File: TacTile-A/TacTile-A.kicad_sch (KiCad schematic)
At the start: 100 parts, among them J1 Conn_01x01, J2 Conn_01x01, J3 Conn_01x01, J4 Conn_01x01, U1 MCP14A0304xMNY, U10 MCP14A0304xMNY, U11 MCP14A0304xMNY, U12 MCP14A0304xMNY, U13 MCP14A0304xMNY, U14 MCP14A0304xMNY, U15 MCP14A0304xMNY, U16 MCP14A0304xMNY, U2 MCP14A0304xMNY, U3 MCP14A0304xMNY, U4 MCP14A0304xMNY, U5 MCP14A0304xMNY, U6 MCP14A0304xMNY, U7 MCP14A0304xMNY, U8 MCP14A0304xMNY, U9 MCP14A0304xMNY

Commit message: Swapped headers and sockets on board A
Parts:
- J1, J3: footprint Connector_PinHeader_2.00mm:PinHeader_1x01_P2.00mm_Horizontal -> Connector_PinSocket_2.00mm:PinSocket_1x01_P2.00mm_Horizontal
- J2, J4: footprint Connector_PinSocket_2.00mm:PinSocket_1x01_P2.00mm_Horizontal -> Connector_PinHeader_2.00mm:PinHeader_1x01_P2.00mm_Horizontal

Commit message: Enlarged grounding pins on board A
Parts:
- J1, J3: footprint Connector_PinSocket_2.00mm:PinSocket_1x01_P2.00mm_Horizontal -> Connector_PinSocket_2.54mm:PinSocket_1x01_P2.54mm_Horizontal
- J2, J4: footprint Connector_PinHeader_2.00mm:PinHeader_1x01_P2.00mm_Horizontal -> Connector_PinHeader_2.54mm:PinHeader_1x01_P2.54mm_Horizontal
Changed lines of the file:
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@@
       (effects (font (size 1.27 1.27)))
     )
-    (property "Footprint" "Connector_PinSocket_2.00mm:PinSocket_1x01_P2.00mm_Horizontal" (at 21.59 218.44 0)
+    (property "Footprint" "Connector_PinSocket_2.54mm:PinSocket_1x01_P2.54mm_Horizontal" (at 21.59 218.44 0)
       (effects (font (size 1.27 1.27)) hide)
     )
@@
       (effects (font (size 1.27 1.27)) (justify left))
     )
-    (property "Footprint" "Connector_PinSocket_2.00mm:PinSocket_1x01_P2.00mm_Horizontal" (at 21.59 214.63 0)
+    (property "Footprint" "Connector_PinSocket_2.54mm:PinSocket_1x01_P2.54mm_Horizontal" (at 21.59 214.63 0)
       (effects (font (size 1.27 1.27)) hide)
     )
@@
       (effects (font (size 1.27 1.27)))
     )
-    (property "Footprint" "Connector_PinHeader_2.00mm:PinHeader_1x01_P2.00mm_Horizontal" (at 45.72 214.63 0)
+    (property "Footprint" "Connector_PinHeader_2.54mm:PinHeader_1x01_P2.54mm_Horizontal" (at 45.72 214.63 0)
       (effects (font (size 1.27 1.27)) hide)
     )
@@
       (effects (font (size 1.27 1.27)))
     )
-    (property "Footprint" "Connector_PinHeader_2.00mm:PinHeader_1x01_P2.00mm_Horizontal" (at 45.72 218.44 0)
+    (property "Footprint" "Connector_PinHeader_2.54mm:PinHeader_1x01_P2.54mm_Horizontal" (at 45.72 218.44 0)
       (effects (font (size 1.27 1.27)) hide)
     )

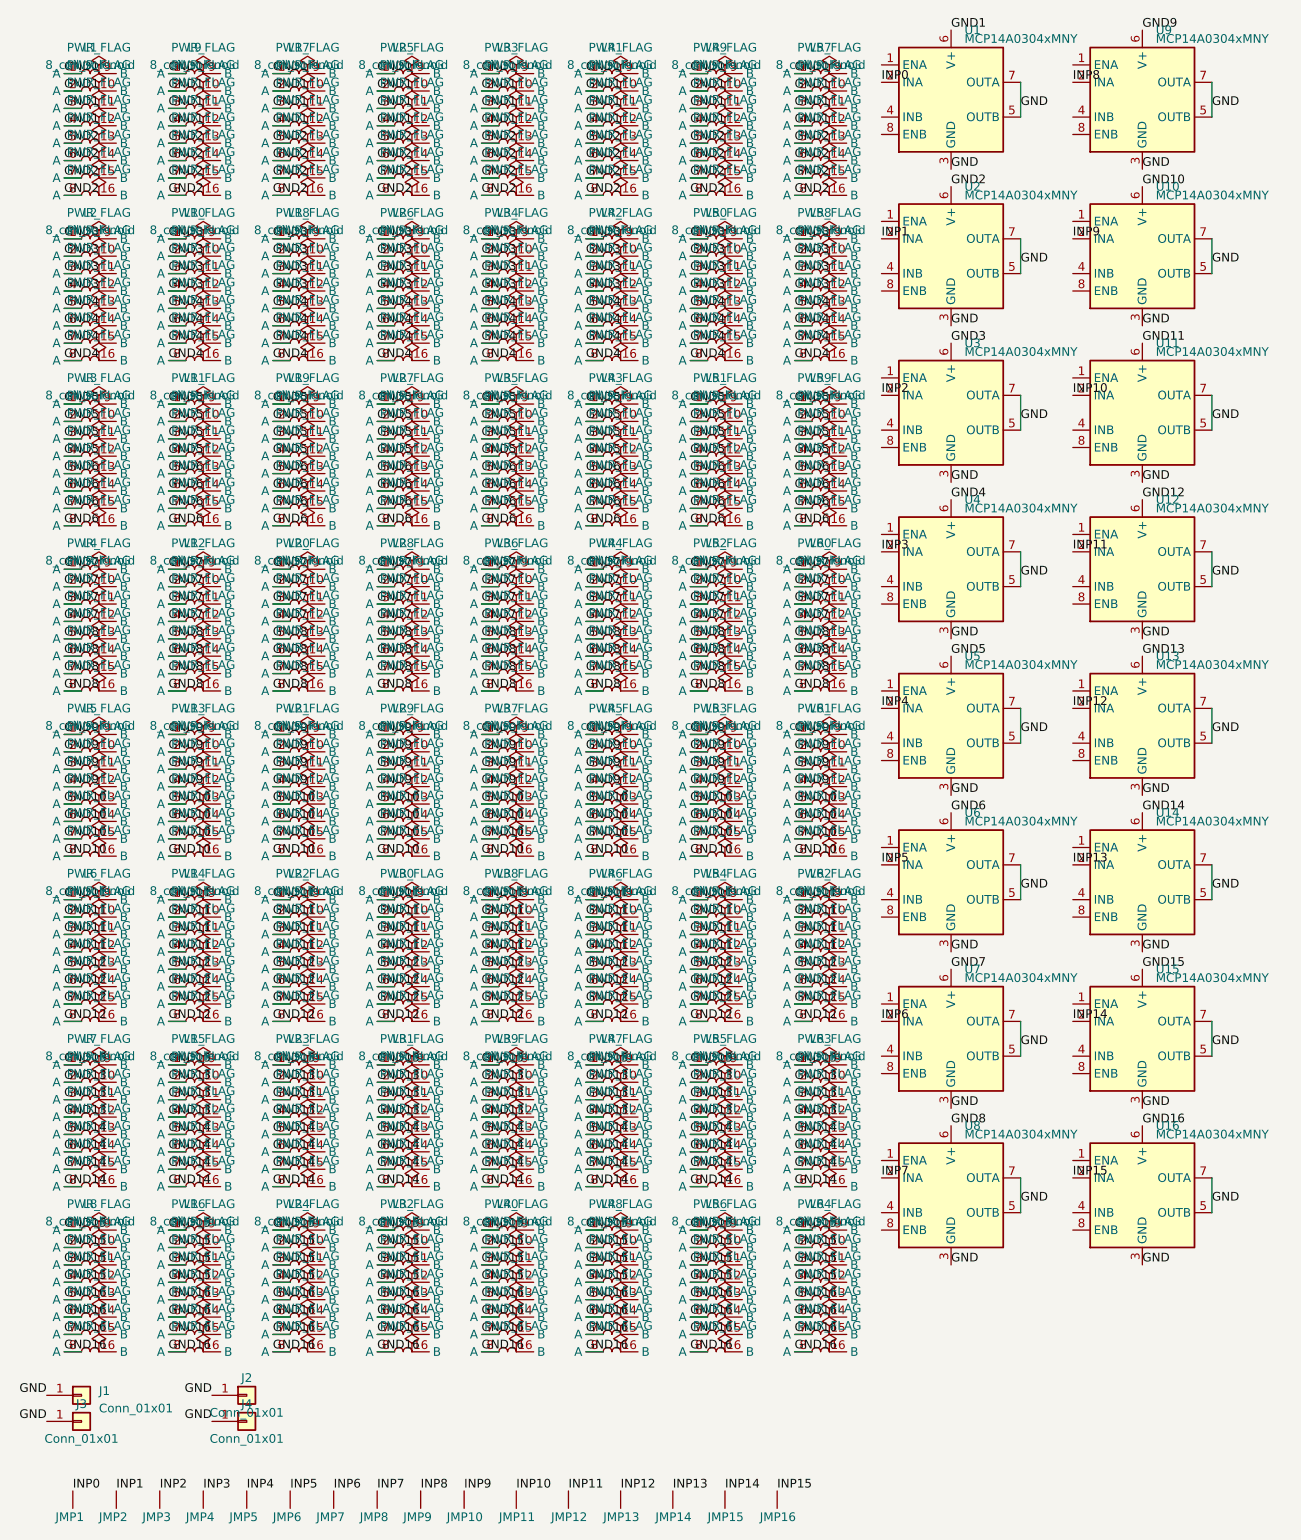
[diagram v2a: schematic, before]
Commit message: Redid A board with MOSFETs sinking current
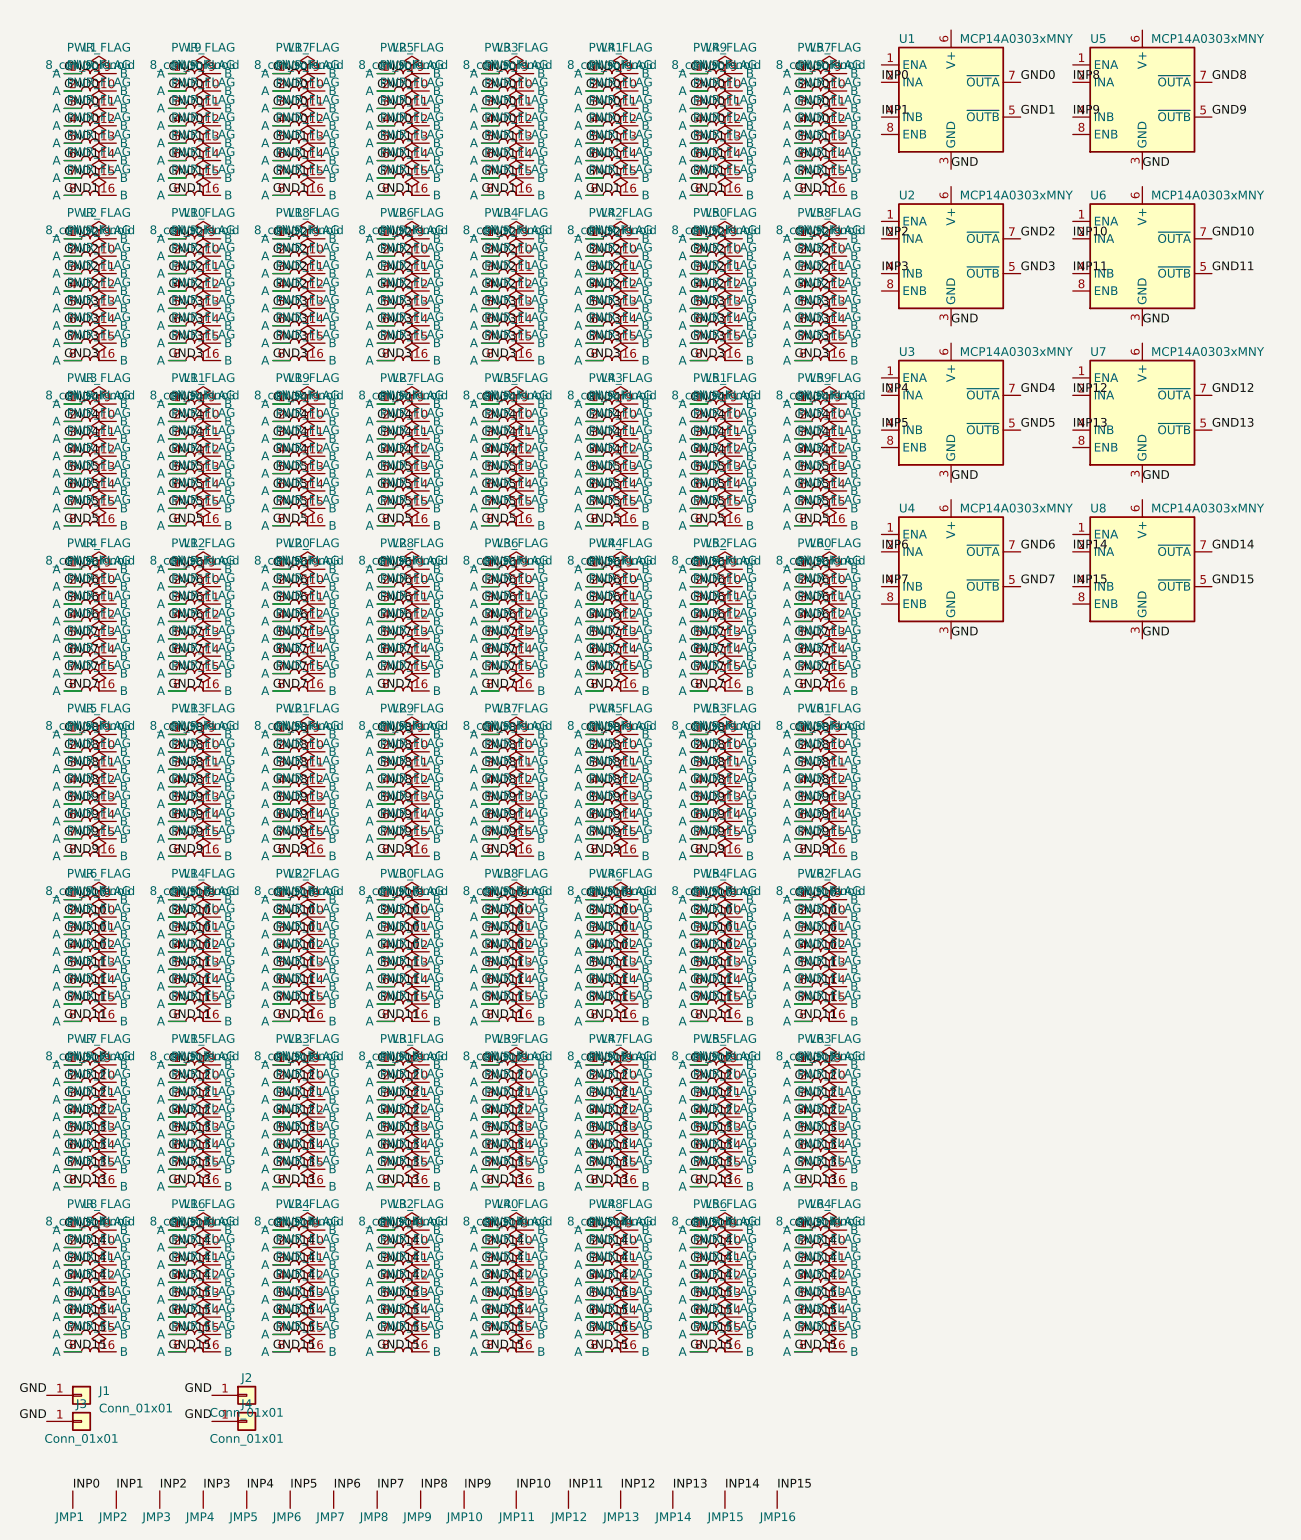
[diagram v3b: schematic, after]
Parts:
- removed U13, U14, U15, U16, U5, U6, U7, U8: MCP14A0304xMNY, Package_DFN_QFN:WDFN-8-1EP_3x2mm_P0.5mm_EP1.3x1.4mm, symbol Driver_FET:MCP14A0304xMNY
- U1, U2, U3, U4: value MCP14A0304xMNY -> MCP14A0303xMNY; symbol Driver_FET:MCP14A0304xMNY -> Driver_FET:MCP14A0303xMNY
- U5: renamed from U9; value MCP14A0304xMNY -> MCP14A0303xMNY; symbol Driver_FET:MCP14A0304xMNY -> Driver_FET:MCP14A0303xMNY
- U6: renamed from U10; value MCP14A0304xMNY -> MCP14A0303xMNY; symbol Driver_FET:MCP14A0304xMNY -> Driver_FET:MCP14A0303xMNY
- U7: renamed from U11; value MCP14A0304xMNY -> MCP14A0303xMNY; symbol Driver_FET:MCP14A0304xMNY -> Driver_FET:MCP14A0303xMNY
- U8: renamed from U12; value MCP14A0304xMNY -> MCP14A0303xMNY; symbol Driver_FET:MCP14A0304xMNY -> Driver_FET:MCP14A0303xMNY
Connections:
- net GND16 is gone; now on net GND15: L16.5 (A), L16.6 (A), L16.7 (A), L16.8 (A), L24.5 (A), L24.6 (A), L24.7 (A), L24.8 (A), L32.5 (A), L32.6 (A), L32.7 (A), L32.8 (A), L40.5 (A), L40.6 (A), L40.7 (A), L40.8 (A), L48.5 (A), L48.6 (A), L48.7 (A), L48.8 (A), L56.5 (A), L56.6 (A), L56.7 (A), L56.8 (A), L64.5 (A), L64.6 (A), L64.7 (A), L64.8 (A), L8.5 (A), L8.6 (A), L8.7 (A), L8.8 (A)
- net GND: no longer U1.5 (OUTB), U1.7 (OUTA), U2.5 (OUTB), U2.7 (OUTA), U3.5 (OUTB), U3.7 (OUTA), U4.5 (OUTB), U4.7 (OUTA), U5.5 (OUTB), U5.7 (OUTA), U6.5 (OUTB), U6.7 (OUTA), U7.5 (OUTB), U7.7 (OUTA), U8.5 (OUTB), U8.7 (OUTA)
- net GND1: now also L1.5 (A), L1.6 (A), L1.7 (A), L1.8 (A), L17.5 (A), L17.6 (A), L17.7 (A), L17.8 (A), L25.5 (A), L25.6 (A), L25.7 (A), L25.8 (A), L33.5 (A), L33.6 (A), L33.7 (A), L33.8 (A), L41.5 (A), L41.6 (A), L41.7 (A), L41.8 (A), L49.5 (A), L49.6 (A), L49.7 (A), L49.8 (A), L57.5 (A), L57.6 (A), L57.7 (A), L57.8 (A), L9.5 (A), L9.6 (A), L9.7 (A), L9.8 (A), U1.5 (~{OUTB}); no longer L1.1 (A), L1.2 (A), L1.3 (A), L1.4 (A), L17.1 (A), L17.2 (A), L17.3 (A), L17.4 (A), L25.1 (A), L25.2 (A), L25.3 (A), L25.4 (A), L33.1 (A), L33.2 (A), L33.3 (A), L33.4 (A), L41.1 (A), L41.2 (A), L41.3 (A), L41.4 (A), L49.1 (A), L49.2 (A), L49.3 (A), L49.4 (A), L57.1 (A), L57.2 (A), L57.3 (A), L57.4 (A), L9.1 (A), L9.2 (A), L9.3 (A), L9.4 (A), U1.6 (V+)
- net GND10: now also L14.1 (A), L14.2 (A), L14.3 (A), L14.4 (A), L22.1 (A), L22.2 (A), L22.3 (A), L22.4 (A), L30.1 (A), L30.2 (A), L30.3 (A), L30.4 (A), L38.1 (A), L38.2 (A), L38.3 (A), L38.4 (A), L46.1 (A), L46.2 (A), L46.3 (A), L46.4 (A), L54.1 (A), L54.2 (A), L54.3 (A), L54.4 (A), L6.1 (A), L6.2 (A), L6.3 (A), L6.4 (A), L62.1 (A), L62.2 (A), L62.3 (A), L62.4 (A), U6.7 (~{OUTA}); no longer L13.5 (A), L13.6 (A), L13.7 (A), L13.8 (A), L21.5 (A), L21.6 (A), L21.7 (A), L21.8 (A), L29.5 (A), L29.6 (A), L29.7 (A), L29.8 (A), L37.5 (A), L37.6 (A), L37.7 (A), L37.8 (A), L45.5 (A), L45.6 (A), L45.7 (A), L45.8 (A), L5.5 (A), L5.6 (A), L5.7 (A), L5.8 (A), L53.5 (A), L53.6 (A), L53.7 (A), L53.8 (A), L61.5 (A), L61.6 (A), L61.7 (A), L61.8 (A), U6.6 (V+)
- net GND11: now also L14.5 (A), L14.6 (A), L14.7 (A), L14.8 (A), L22.5 (A), L22.6 (A), L22.7 (A), L22.8 (A), L30.5 (A), L30.6 (A), L30.7 (A), L30.8 (A), L38.5 (A), L38.6 (A), L38.7 (A), L38.8 (A), L46.5 (A), L46.6 (A), L46.7 (A), L46.8 (A), L54.5 (A), L54.6 (A), L54.7 (A), L54.8 (A), L6.5 (A), L6.6 (A), L6.7 (A), L6.8 (A), L62.5 (A), L62.6 (A), L62.7 (A), L62.8 (A), U6.5 (~{OUTB}); no longer L14.1 (A), L14.2 (A), L14.3 (A), L14.4 (A), L22.1 (A), L22.2 (A), L22.3 (A), L22.4 (A), L30.1 (A), L30.2 (A), L30.3 (A), L30.4 (A), L38.1 (A), L38.2 (A), L38.3 (A), L38.4 (A), L46.1 (A), L46.2 (A), L46.3 (A), L46.4 (A), L54.1 (A), L54.2 (A), L54.3 (A), L54.4 (A), L6.1 (A), L6.2 (A), L6.3 (A), L6.4 (A), L62.1 (A), L62.2 (A), L62.3 (A), L62.4 (A), U7.6 (V+)
- net GND12: now also L15.1 (A), L15.2 (A), L15.3 (A), L15.4 (A), L23.1 (A), L23.2 (A), L23.3 (A), L23.4 (A), L31.1 (A), L31.2 (A), L31.3 (A), L31.4 (A), L39.1 (A), L39.2 (A), L39.3 (A), L39.4 (A), L47.1 (A), L47.2 (A), L47.3 (A), L47.4 (A), L55.1 (A), L55.2 (A), L55.3 (A), L55.4 (A), L63.1 (A), L63.2 (A), L63.3 (A), L63.4 (A), L7.1 (A), L7.2 (A), L7.3 (A), L7.4 (A), U7.7 (~{OUTA}); no longer L14.5 (A), L14.6 (A), L14.7 (A), L14.8 (A), L22.5 (A), L22.6 (A), L22.7 (A), L22.8 (A), L30.5 (A), L30.6 (A), L30.7 (A), L30.8 (A), L38.5 (A), L38.6 (A), L38.7 (A), L38.8 (A), L46.5 (A), L46.6 (A), L46.7 (A), L46.8 (A), L54.5 (A), L54.6 (A), L54.7 (A), L54.8 (A), L6.5 (A), L6.6 (A), L6.7 (A), L6.8 (A), L62.5 (A), L62.6 (A), L62.7 (A), L62.8 (A), U8.6 (V+)
- net GND13: now also L15.5 (A), L15.6 (A), L15.7 (A), L15.8 (A), L23.5 (A), L23.6 (A), L23.7 (A), L23.8 (A), L31.5 (A), L31.6 (A), L31.7 (A), L31.8 (A), L39.5 (A), L39.6 (A), L39.7 (A), L39.8 (A), L47.5 (A), L47.6 (A), L47.7 (A), L47.8 (A), L55.5 (A), L55.6 (A), L55.7 (A), L55.8 (A), L63.5 (A), L63.6 (A), L63.7 (A), L63.8 (A), L7.5 (A), L7.6 (A), L7.7 (A), L7.8 (A), U7.5 (~{OUTB}); no longer L15.1 (A), L15.2 (A), L15.3 (A), L15.4 (A), L23.1 (A), L23.2 (A), L23.3 (A), L23.4 (A), L31.1 (A), L31.2 (A), L31.3 (A), L31.4 (A), L39.1 (A), L39.2 (A), L39.3 (A), L39.4 (A), L47.1 (A), L47.2 (A), L47.3 (A), L47.4 (A), L55.1 (A), L55.2 (A), L55.3 (A), L55.4 (A), L63.1 (A), L63.2 (A), L63.3 (A), L63.4 (A), L7.1 (A), L7.2 (A), L7.3 (A), L7.4 (A)
- net GND14: now also L16.1 (A), L16.2 (A), L16.3 (A), L16.4 (A), L24.1 (A), L24.2 (A), L24.3 (A), L24.4 (A), L32.1 (A), L32.2 (A), L32.3 (A), L32.4 (A), L40.1 (A), L40.2 (A), L40.3 (A), L40.4 (A), L48.1 (A), L48.2 (A), L48.3 (A), L48.4 (A), L56.1 (A), L56.2 (A), L56.3 (A), L56.4 (A), L64.1 (A), L64.2 (A), L64.3 (A), L64.4 (A), L8.1 (A), L8.2 (A), L8.3 (A), L8.4 (A), U8.7 (~{OUTA}); no longer L15.5 (A), L15.6 (A), L15.7 (A), L15.8 (A), L23.5 (A), L23.6 (A), L23.7 (A), L23.8 (A), L31.5 (A), L31.6 (A), L31.7 (A), L31.8 (A), L39.5 (A), L39.6 (A), L39.7 (A), L39.8 (A), L47.5 (A), L47.6 (A), L47.7 (A), L47.8 (A), L55.5 (A), L55.6 (A), L55.7 (A), L55.8 (A), L63.5 (A), L63.6 (A), L63.7 (A), L63.8 (A), L7.5 (A), L7.6 (A), L7.7 (A), L7.8 (A)
- net GND15: now also U8.5 (~{OUTB}); no longer L16.1 (A), L16.2 (A), L16.3 (A), L16.4 (A), L24.1 (A), L24.2 (A), L24.3 (A), L24.4 (A), L32.1 (A), L32.2 (A), L32.3 (A), L32.4 (A), L40.1 (A), L40.2 (A), L40.3 (A), L40.4 (A), L48.1 (A), L48.2 (A), L48.3 (A), L48.4 (A), L56.1 (A), L56.2 (A), L56.3 (A), L56.4 (A), L64.1 (A), L64.2 (A), L64.3 (A), L64.4 (A), L8.1 (A), L8.2 (A), L8.3 (A), L8.4 (A)
- net GND2: now also L10.1 (A), L10.2 (A), L10.3 (A), L10.4 (A), L18.1 (A), L18.2 (A), L18.3 (A), L18.4 (A), L2.1 (A), L2.2 (A), L2.3 (A), L2.4 (A), L26.1 (A), L26.2 (A), L26.3 (A), L26.4 (A), L34.1 (A), L34.2 (A), L34.3 (A), L34.4 (A), L42.1 (A), L42.2 (A), L42.3 (A), L42.4 (A), L50.1 (A), L50.2 (A), L50.3 (A), L50.4 (A), L58.1 (A), L58.2 (A), L58.3 (A), L58.4 (A), U2.7 (~{OUTA}); no longer L1.5 (A), L1.6 (A), L1.7 (A), L1.8 (A), L17.5 (A), L17.6 (A), L17.7 (A), L17.8 (A), L25.5 (A), L25.6 (A), L25.7 (A), L25.8 (A), L33.5 (A), L33.6 (A), L33.7 (A), L33.8 (A), L41.5 (A), L41.6 (A), L41.7 (A), L41.8 (A), L49.5 (A), L49.6 (A), L49.7 (A), L49.8 (A), L57.5 (A), L57.6 (A), L57.7 (A), L57.8 (A), L9.5 (A), L9.6 (A), L9.7 (A), L9.8 (A), U2.6 (V+)
- net GND3: now also L10.5 (A), L10.6 (A), L10.7 (A), L10.8 (A), L18.5 (A), L18.6 (A), L18.7 (A), L18.8 (A), L2.5 (A), L2.6 (A), L2.7 (A), L2.8 (A), L26.5 (A), L26.6 (A), L26.7 (A), L26.8 (A), L34.5 (A), L34.6 (A), L34.7 (A), L34.8 (A), L42.5 (A), L42.6 (A), L42.7 (A), L42.8 (A), L50.5 (A), L50.6 (A), L50.7 (A), L50.8 (A), L58.5 (A), L58.6 (A), L58.7 (A), L58.8 (A), U2.5 (~{OUTB}); no longer L10.1 (A), L10.2 (A), L10.3 (A), L10.4 (A), L18.1 (A), L18.2 (A), L18.3 (A), L18.4 (A), L2.1 (A), L2.2 (A), L2.3 (A), L2.4 (A), L26.1 (A), L26.2 (A), L26.3 (A), L26.4 (A), L34.1 (A), L34.2 (A), L34.3 (A), L34.4 (A), L42.1 (A), L42.2 (A), L42.3 (A), L42.4 (A), L50.1 (A), L50.2 (A), L50.3 (A), L50.4 (A), L58.1 (A), L58.2 (A), L58.3 (A), L58.4 (A), U3.6 (V+)
- net GND4: now also L11.1 (A), L11.2 (A), L11.3 (A), L11.4 (A), L19.1 (A), L19.2 (A), L19.3 (A), L19.4 (A), L27.1 (A), L27.2 (A), L27.3 (A), L27.4 (A), L3.1 (A), L3.2 (A), L3.3 (A), L3.4 (A), L35.1 (A), L35.2 (A), L35.3 (A), L35.4 (A), L43.1 (A), L43.2 (A), L43.3 (A), L43.4 (A), L51.1 (A), L51.2 (A), L51.3 (A), L51.4 (A), L59.1 (A), L59.2 (A), L59.3 (A), L59.4 (A), U3.7 (~{OUTA}); no longer L10.5 (A), L10.6 (A), L10.7 (A), L10.8 (A), L18.5 (A), L18.6 (A), L18.7 (A), L18.8 (A), L2.5 (A), L2.6 (A), L2.7 (A), L2.8 (A), L26.5 (A), L26.6 (A), L26.7 (A), L26.8 (A), L34.5 (A), L34.6 (A), L34.7 (A), L34.8 (A), L42.5 (A), L42.6 (A), L42.7 (A), L42.8 (A), L50.5 (A), L50.6 (A), L50.7 (A), L50.8 (A), L58.5 (A), L58.6 (A), L58.7 (A), L58.8 (A), U4.6 (V+)
- net GND5: now also L11.5 (A), L11.6 (A), L11.7 (A), L11.8 (A), L19.5 (A), L19.6 (A), L19.7 (A), L19.8 (A), L27.5 (A), L27.6 (A), L27.7 (A), L27.8 (A), L3.5 (A), L3.6 (A), L3.7 (A), L3.8 (A), L35.5 (A), L35.6 (A), L35.7 (A), L35.8 (A), L43.5 (A), L43.6 (A), L43.7 (A), L43.8 (A), L51.5 (A), L51.6 (A), L51.7 (A), L51.8 (A), L59.5 (A), L59.6 (A), L59.7 (A), L59.8 (A), U3.5 (~{OUTB}); no longer L11.1 (A), L11.2 (A), L11.3 (A), L11.4 (A), L19.1 (A), L19.2 (A), L19.3 (A), L19.4 (A), L27.1 (A), L27.2 (A), L27.3 (A), L27.4 (A), L3.1 (A), L3.2 (A), L3.3 (A), L3.4 (A), L35.1 (A), L35.2 (A), L35.3 (A), L35.4 (A), L43.1 (A), L43.2 (A), L43.3 (A), L43.4 (A), L51.1 (A), L51.2 (A), L51.3 (A), L51.4 (A), L59.1 (A), L59.2 (A), L59.3 (A), L59.4 (A)
- net GND6: now also L12.1 (A), L12.2 (A), L12.3 (A), L12.4 (A), L20.1 (A), L20.2 (A), L20.3 (A), L20.4 (A), L28.1 (A), L28.2 (A), L28.3 (A), L28.4 (A), L36.1 (A), L36.2 (A), L36.3 (A), L36.4 (A), L4.1 (A), L4.2 (A), L4.3 (A), L4.4 (A), L44.1 (A), L44.2 (A), L44.3 (A), L44.4 (A), L52.1 (A), L52.2 (A), L52.3 (A), L52.4 (A), L60.1 (A), L60.2 (A), L60.3 (A), L60.4 (A), U4.7 (~{OUTA}); no longer L11.5 (A), L11.6 (A), L11.7 (A), L11.8 (A), L19.5 (A), L19.6 (A), L19.7 (A), L19.8 (A), L27.5 (A), L27.6 (A), L27.7 (A), L27.8 (A), L3.5 (A), L3.6 (A), L3.7 (A), L3.8 (A), L35.5 (A), L35.6 (A), L35.7 (A), L35.8 (A), L43.5 (A), L43.6 (A), L43.7 (A), L43.8 (A), L51.5 (A), L51.6 (A), L51.7 (A), L51.8 (A), L59.5 (A), L59.6 (A), L59.7 (A), L59.8 (A)
- net GND7: now also L12.5 (A), L12.6 (A), L12.7 (A), L12.8 (A), L20.5 (A), L20.6 (A), L20.7 (A), L20.8 (A), L28.5 (A), L28.6 (A), L28.7 (A), L28.8 (A), L36.5 (A), L36.6 (A), L36.7 (A), L36.8 (A), L4.5 (A), L4.6 (A), L4.7 (A), L4.8 (A), L44.5 (A), L44.6 (A), L44.7 (A), L44.8 (A), L52.5 (A), L52.6 (A), L52.7 (A), L52.8 (A), L60.5 (A), L60.6 (A), L60.7 (A), L60.8 (A), U4.5 (~{OUTB}); no longer L12.1 (A), L12.2 (A), L12.3 (A), L12.4 (A), L20.1 (A), L20.2 (A), L20.3 (A), L20.4 (A), L28.1 (A), L28.2 (A), L28.3 (A), L28.4 (A), L36.1 (A), L36.2 (A), L36.3 (A), L36.4 (A), L4.1 (A), L4.2 (A), L4.3 (A), L4.4 (A), L44.1 (A), L44.2 (A), L44.3 (A), L44.4 (A), L52.1 (A), L52.2 (A), L52.3 (A), L52.4 (A), L60.1 (A), L60.2 (A), L60.3 (A), L60.4 (A)
- net GND8: now also L13.1 (A), L13.2 (A), L13.3 (A), L13.4 (A), L21.1 (A), L21.2 (A), L21.3 (A), L21.4 (A), L29.1 (A), L29.2 (A), L29.3 (A), L29.4 (A), L37.1 (A), L37.2 (A), L37.3 (A), L37.4 (A), L45.1 (A), L45.2 (A), L45.3 (A), L45.4 (A), L5.1 (A), L5.2 (A), L5.3 (A), L5.4 (A), L53.1 (A), L53.2 (A), L53.3 (A), L53.4 (A), L61.1 (A), L61.2 (A), L61.3 (A), L61.4 (A), U5.7 (~{OUTA}); no longer L12.5 (A), L12.6 (A), L12.7 (A), L12.8 (A), L20.5 (A), L20.6 (A), L20.7 (A), L20.8 (A), L28.5 (A), L28.6 (A), L28.7 (A), L28.8 (A), L36.5 (A), L36.6 (A), L36.7 (A), L36.8 (A), L4.5 (A), L4.6 (A), L4.7 (A), L4.8 (A), L44.5 (A), L44.6 (A), L44.7 (A), L44.8 (A), L52.5 (A), L52.6 (A), L52.7 (A), L52.8 (A), L60.5 (A), L60.6 (A), L60.7 (A), L60.8 (A)
- net GND9: now also L13.5 (A), L13.6 (A), L13.7 (A), L13.8 (A), L21.5 (A), L21.6 (A), L21.7 (A), L21.8 (A), L29.5 (A), L29.6 (A), L29.7 (A), L29.8 (A), L37.5 (A), L37.6 (A), L37.7 (A), L37.8 (A), L45.5 (A), L45.6 (A), L45.7 (A), L45.8 (A), L5.5 (A), L5.6 (A), L5.7 (A), L5.8 (A), L53.5 (A), L53.6 (A), L53.7 (A), L53.8 (A), L61.5 (A), L61.6 (A), L61.7 (A), L61.8 (A), U5.5 (~{OUTB}); no longer L13.1 (A), L13.2 (A), L13.3 (A), L13.4 (A), L21.1 (A), L21.2 (A), L21.3 (A), L21.4 (A), L29.1 (A), L29.2 (A), L29.3 (A), L29.4 (A), L37.1 (A), L37.2 (A), L37.3 (A), L37.4 (A), L45.1 (A), L45.2 (A), L45.3 (A), L45.4 (A), L5.1 (A), L5.2 (A), L5.3 (A), L5.4 (A), L53.1 (A), L53.2 (A), L53.3 (A), L53.4 (A), L61.1 (A), L61.2 (A), L61.3 (A), L61.4 (A), U5.6 (V+)
- net INP1: now also U1.4 (INB); no longer U2.2 (INA)
- net INP10: now also U6.2 (INA); no longer U7.2 (INA)
- net INP11: now also U6.4 (INB); no longer U8.2 (INA)
- net INP12: now also U7.2 (INA)
- net INP13: now also U7.4 (INB)
- net INP14: now also U8.2 (INA)
- net INP15: now also U8.4 (INB)
- net INP2: now also U2.2 (INA); no longer U3.2 (INA)
- net INP3: now also U2.4 (INB); no longer U4.2 (INA)
- net INP4: now also U3.2 (INA)
- net INP5: now also U3.4 (INB)
- net INP6: now also U4.2 (INA)
- net INP7: now also U4.4 (INB)
- net INP9: now also U5.4 (INB); no longer U6.2 (INA)
- new net GND0: L1.1 (A), L1.2 (A), L1.3 (A), L1.4 (A), L17.1 (A), L17.2 (A), L17.3 (A), L17.4 (A), L25.1 (A), L25.2 (A), L25.3 (A), L25.4 (A), L33.1 (A), L33.2 (A), L33.3 (A), L33.4 (A), L41.1 (A), L41.2 (A), L41.3 (A), L41.4 (A), L49.1 (A), L49.2 (A), L49.3 (A), L49.4 (A), L57.1 (A), L57.2 (A), L57.3 (A), L57.4 (A), L9.1 (A), L9.2 (A), L9.3 (A), L9.4 (A), U1.7 (~{OUTA})
